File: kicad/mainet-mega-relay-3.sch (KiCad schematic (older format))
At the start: 8 parts, among them J32 Screw_Terminal_01x03, K3 SANYOU_SRD_Form_C, Q3 2N3904, U4 4N37

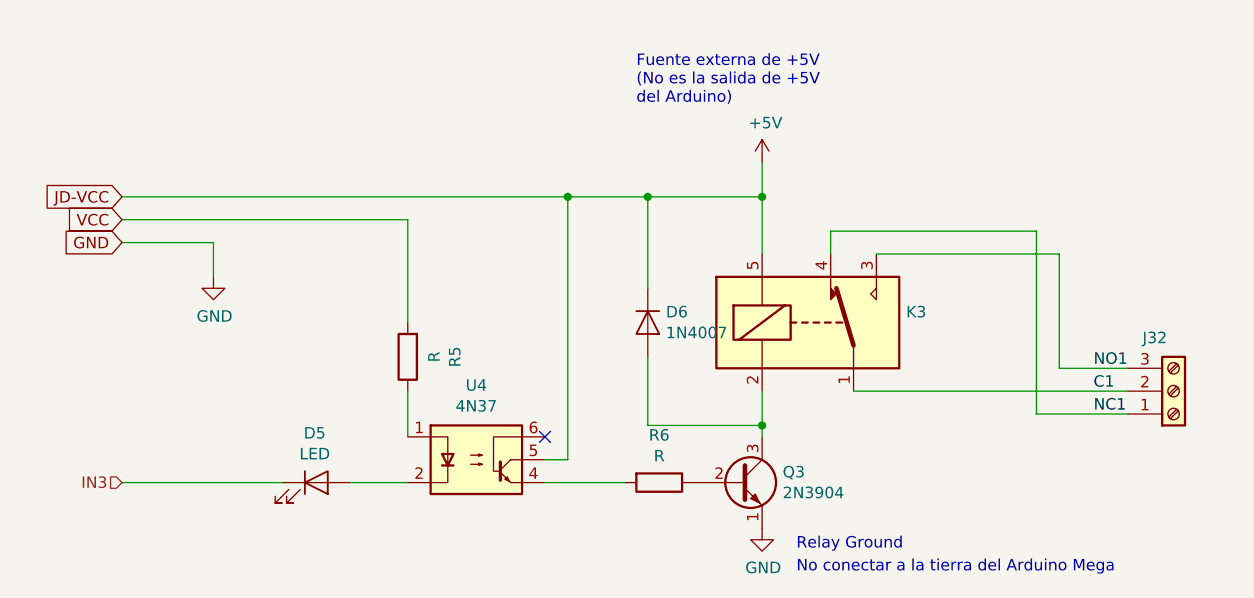
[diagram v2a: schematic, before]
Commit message: KICAD: Actualización de esquematicos del módulo de 8 relés de control
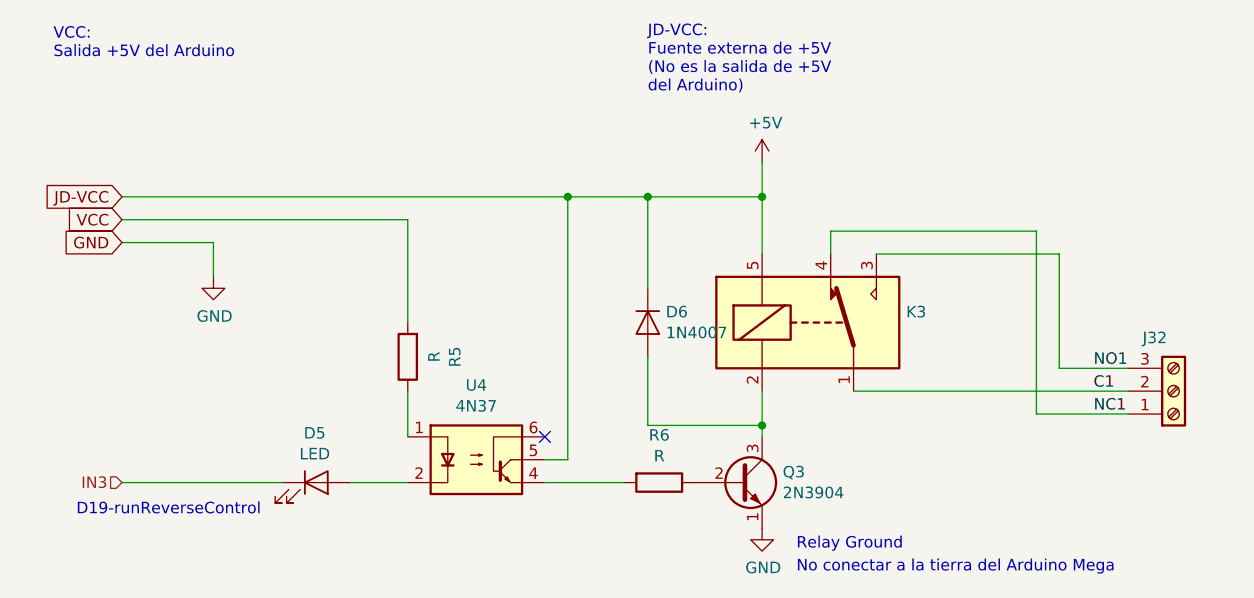
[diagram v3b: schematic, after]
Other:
- note added: "D19-runReverseControl"
- note added: "JD-VCC:\nFuente externa de +5V\n(No es la salida de +5V \ndel Arduino)"
- note added: "VCC:\nSalida +5V del Arduino"
- note removed: "Fuente externa de +5V\n(No es la salida de +5V \ndel Arduino)"
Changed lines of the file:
@@
 EESchema Schematic File Version 4
 LIBS:mainet-mega-cache
-LIBS:mainet-mega-5V-to-mp-10v-cache
 EELAYER 30 0
 EELAYER END
 $Descr A4 11693 8268
 encoding utf-8
-Sheet 8 21
-Title ""
-Date ""
+Sheet 9 21
+Title "Relay driver 3"
+Date "2021-02-02"
 Rev ""
 Comp ""
@@
 	1    0    0    -1
 $EndComp
-Text Notes 5950 2650 0    50   ~ 0
-Fuente externa de +5V\n(No es la salida de +5V \ndel Arduino)
 Text Notes 6650 4600 0    50   ~ 0
 Relay Ground\n
@@
 Text GLabel 3700 3250 0    50   Input ~ 0
 GND
+Text Notes 6000 2600 0    50   ~ 0
+JD-VCC:\nFuente externa de +5V\n(No es la salida de +5V \ndel Arduino)
+Text Notes 3400 2450 0    50   ~ 0
+VCC:\nSalida +5V del Arduino
+Text Notes 3500 4450 0    50   ~ 0
+D19-runReverseControl
 $EndSCHEMATC
